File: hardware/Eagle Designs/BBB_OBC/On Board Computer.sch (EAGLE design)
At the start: 25 parts, among them J1 MOLEX_503763-0491MOLEX_503763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, J10 503763-0591, J11 503763-0591, J12 503763-0691, J13 MOLEX_503763-0291MOLEX_503763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, J14 MOLEX_503763-0491MOLEX_503763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, J15 MOLEX_503763-0491MOLEX_503763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, J2 MOLEX_503763-0491MOLEX_503763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, J3 503763-0591, J4 503763-0591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

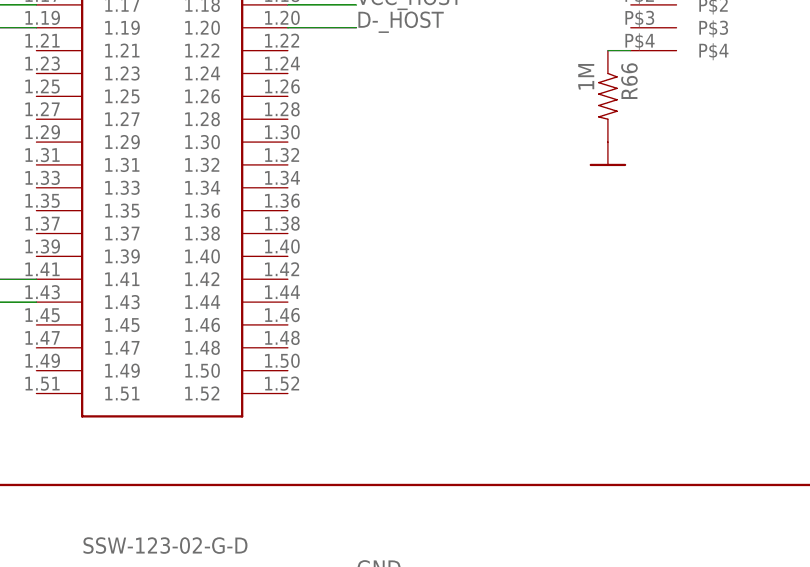
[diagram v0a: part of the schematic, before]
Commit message: Edited payload board, created payload and bbb obc BOM
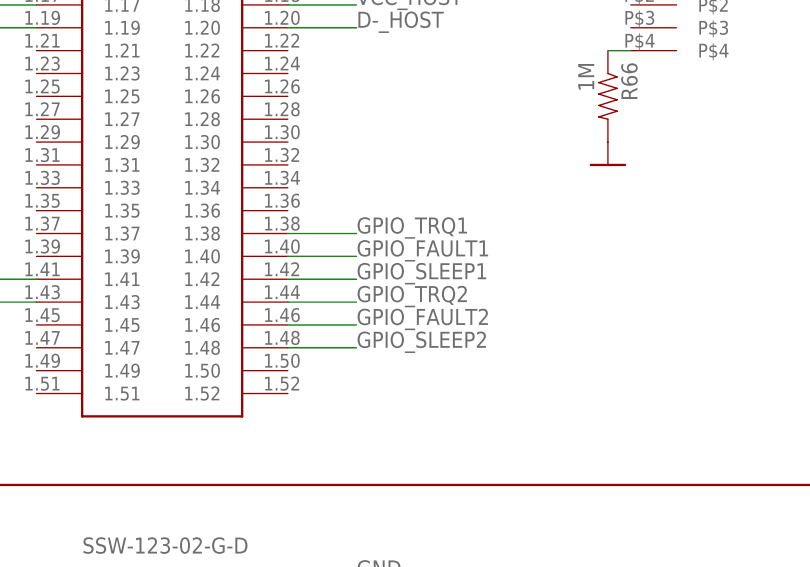
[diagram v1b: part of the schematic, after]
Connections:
- new net GPIO_FAULT1: H1.1.40
- new net GPIO_FAULT2: H1.1.46
- new net GPIO_SLEEP1: H1.1.42
- new net GPIO_SLEEP2: H1.1.48
- new net GPIO_TRQ1: H1.1.38
- new net GPIO_TRQ2: H1.1.44
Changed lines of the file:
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@@
+</segment>
+</net>
+<net name="GPIO_FAULT1" class="0">
+<segment>
+<wire x1="88.9" y1="165.1" x2="96.52" y2="165.1" width="0.1524" layer="91"/>
+<label x="96.52" y="165.1" size="1.778" layer="95"/>
+<pinref part="H1" gate="G$1" pin="1.40"/>
+</segment>
+</net>
+<net name="GPIO_SLEEP1" class="0">
+<segment>
+<wire x1="88.9" y1="162.56" x2="96.52" y2="162.56" width="0.1524" layer="91"/>
+<label x="96.52" y="162.56" size="1.778" layer="95"/>
+<pinref part="H1" gate="G$1" pin="1.42"/>
+</segment>
+</net>
+<net name="GPIO_TRQ1" class="0">
+<segment>
+<wire x1="88.9" y1="167.64" x2="96.52" y2="167.64" width="0.1524" layer="91"/>
+<label x="96.52" y="167.64" size="1.778" layer="95"/>
+<pinref part="H1" gate="G$1" pin="1.38"/>
+</segment>
+</net>
+<net name="GPIO_FAULT2" class="0">
+<segment>
+<wire x1="88.9" y1="157.48" x2="96.52" y2="157.48" width="0.1524" layer="91"/>
+<label x="96.52" y="157.48" size="1.778" layer="95"/>
+<pinref part="H1" gate="G$1" pin="1.46"/>
+</segment>
+</net>
+<net name="GPIO_SLEEP2" class="0">
+<segment>
+<wire x1="88.9" y1="154.94" x2="96.52" y2="154.94" width="0.1524" layer="91"/>
+<label x="96.52" y="154.94" size="1.778" layer="95"/>
+<pinref part="H1" gate="G$1" pin="1.48"/>
+</segment>
+</net>
+<net name="GPIO_TRQ2" class="0">
+<segment>
+<wire x1="88.9" y1="160.02" x2="96.52" y2="160.02" width="0.1524" layer="91"/>
+<label x="96.52" y="160.02" size="1.778" layer="95"/>
+<pinref part="H1" gate="G$1" pin="1.44"/>
 </segment>
 </net>
